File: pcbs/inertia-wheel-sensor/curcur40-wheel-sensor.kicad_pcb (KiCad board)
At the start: 2 copper layers, 8.8 x 8.8 mm, 4 parts, among them J1 SolderPads_1x04, U1 AS5600-ASOT

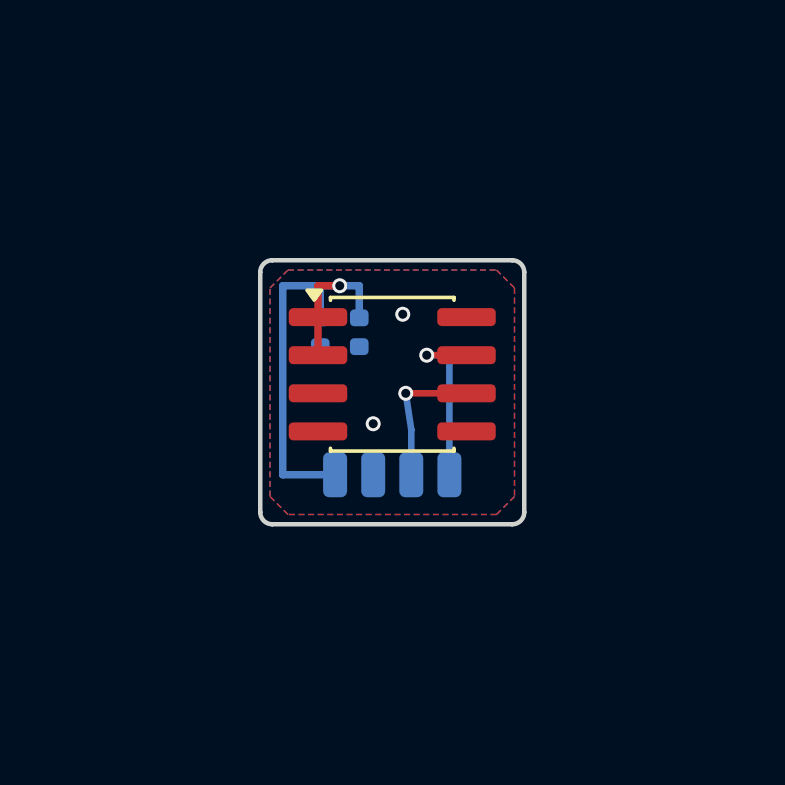
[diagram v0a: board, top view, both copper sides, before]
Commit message: feat(pcb,cad): upgrade curcur40-wheel-sensor to 22x22mm breakaway frame for single-sided JLCPCB Economic PCBA
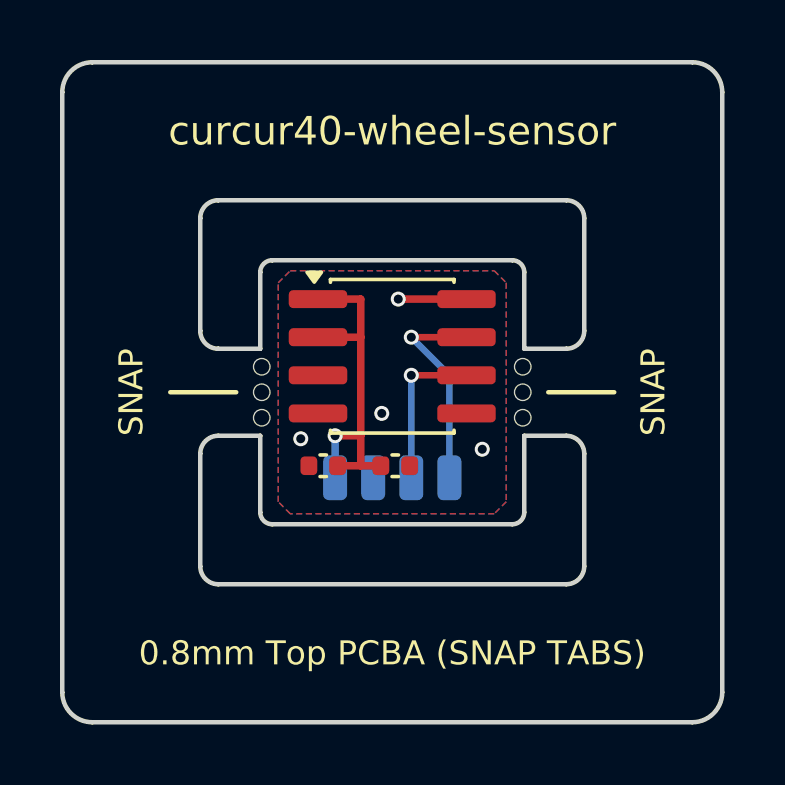
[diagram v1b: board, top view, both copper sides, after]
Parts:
- added MB1: MouseBite, kbd:MouseBite_3x0.55mm, F.Cu at (95.7, 100.0)
- added MB2: MouseBite, kbd:MouseBite_3x0.55mm, F.Cu at (104.3, 100.0)
- C1, C2: moved to F.Cu
- moved C2 4.61 mm to (100.1, 102.5), turned to 0 degrees
- moved C1 4.45 mm to (97.7, 102.5), turned to 180 degrees
- moved U1 0.60 mm to (100.0, 98.8)
- moved J1 0.10 mm to (100.0, 102.8)
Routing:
- net +3V3: track 15.8 -> 12.1 mm
- net GND: track 0.00 -> 2.27 mm, vias 2 -> 4
- net /SCL: track 6.06 -> 7.05 mm
- net /SDA: track 4.75 -> 5.25 mm
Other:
- board size 8.8 x 8.8 mm -> 22 x 22 mm
- board text added: "0.8mm Top PCBA (SNAP TABS)"
- board text added: "3V3"
- board text added: "4:SCL 3:SDA 2:GND 1:3V3"
- board text added: "SCL"
- board text added: "SNAP"
- board text added: "curcur40-wheel-sensor"

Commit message: feat(pcb): trim wheel-sensor upper outline for pyramid cover and align eval SW1
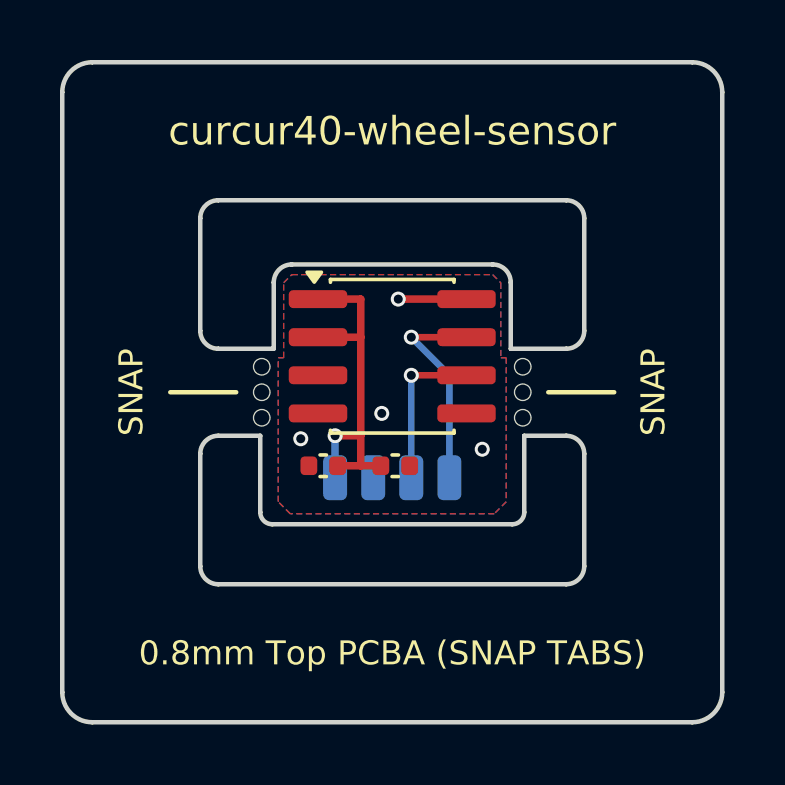
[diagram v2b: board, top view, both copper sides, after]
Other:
- outline, holes or cut-outs redrawn
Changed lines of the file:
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@@
 	(gr_line
 		(start 94.2 98.55)
-		(end 95.6 98.55)
+		(end 96.05 98.55)
 		(stroke
 			(width 0.15)
@@
 		(layer "Edge.Cuts")
 	)
-	(gr_arc
-		(start 95.6 96)
-		(mid 95.717157 95.717157)
-		(end 96 95.6)
-		(stroke
-			(width 0.15)
-			(type default)
-		)
-		(layer "Edge.Cuts")
-	)
-	(gr_line
-		(start 95.6 98.55)
-		(end 95.6 96)
-		(stroke
-			(width 0.15)
-			(type default)
-		)
-		(layer "Edge.Cuts")
-	)
 	(gr_line
 		(start 95.6 101.45)
 		(end 95.6 104)
-		(stroke
-			(width 0.15)
-			(type default)
-		)
-		(layer "Edge.Cuts")
-	)
-	(gr_line
-		(start 96 95.6)
-		(end 104 95.6)
 		(stroke
 			(width 0.15)
@@
 	)
 	(gr_arc
-		(start 104 95.6)
-		(mid 104.282843 95.717157)
-		(end 104.4 96)
-		(stroke
-			(width 0.15)
-			(type default)
-		)
-		(layer "Edge.Cuts")
-	)
-	(gr_line
-		(start 104.4 96)
-		(end 104.4 98.55)
-		(stroke
-			(width 0.15)
-			(type default)
-		)
-		(layer "Edge.Cuts")
-	)
-	(gr_line
-		(start 104.4 98.55)
+		(start 96.05 96.34)
+		(mid 96.225735 95.915735)
+		(end 96.65 95.74)
+		(stroke
+			(width 0.15)
+			(type default)
+		)
+		(layer "Edge.Cuts")
+	)
+	(gr_line
+		(start 96.05 98.55)
+		(end 96.05 96.34)
+		(stroke
+			(width 0.15)
+			(type default)
+		)
+		(layer "Edge.Cuts")
+	)
+	(gr_line
+		(start 96.65 95.74)
+		(end 103.35 95.74)
+		(stroke
+			(width 0.15)
+			(type default)
+		)
+		(layer "Edge.Cuts")
+	)
+	(gr_arc
+		(start 103.35 95.74)
+		(mid 103.774264 95.915735)
+		(end 103.949999 96.34)
+		(stroke
+			(width 0.15)
+			(type default)
+		)
+		(layer "Edge.Cuts")
+	)
+	(gr_line
+		(start 103.95 98.55)
+		(end 103.95 96.34)
+		(stroke
+			(width 0.15)
+			(type default)
+		)
+		(layer "Edge.Cuts")
+	)
+	(gr_line
+		(start 103.95 98.55)
 		(end 105.8 98.55)
 		(stroke
@@
 		(polygon
 			(pts
-				(xy 96.6 95.95) (xy 103.4 95.95) (xy 103.8 96.35) (xy 103.8 103.65) (xy 103.4 104.05) (xy 96.6 104.05)
-				(xy 96.2 103.65) (xy 96.2 96.35)
+				(xy 96.65 96.08) (xy 103.35 96.08) (xy 103.62 96.35) (xy 103.62 98.85) (xy 103.8 98.85) (xy 103.8 103.65)
+				(xy 103.4 104.05) (xy 96.6 104.05) (xy 96.2 103.65) (xy 96.2 98.85) (xy 96.38 98.85) (xy 96.38 96.35)
 			)
 		)
@@
 		(polygon
 			(pts
-				(xy 96.6 95.95) (xy 103.4 95.95) (xy 103.8 96.35) (xy 103.8 103.65) (xy 103.4 104.05) (xy 96.6 104.05)
-				(xy 96.2 103.65) (xy 96.2 96.35)
-			)
-		)
+				(xy 96.65 96.08) (xy 103.35 96.08) (xy 103.62 96.35) (xy 103.62 98.85) (xy 103.8 98.85) (xy 103.8 103.65)
+				(xy 103.4 104.05) (xy 96.6 104.05) (xy 96.2 103.65) (xy 96.2 98.85) (xy 96.38 98.85) (xy 96.38 96.35)
+			)
+		)
